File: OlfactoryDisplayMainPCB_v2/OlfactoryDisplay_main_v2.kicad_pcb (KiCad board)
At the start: 2 copper layers, 62 x 34.5 mm, 25 parts, among them J1 B2B-PH-K-S, J2 B2B-PH-K-S, J3 B2B-PH-K-S, J4 B2B-PH-K-S, J5 B2B-PH-K-S, J6 B2B-PH-K-S, J7 B2B-PH-K-S, J9 B2B-PH-K-S, U1 DMG1012UW-7, U2 DMG1012UW-7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

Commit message: rough draft of traces for V2
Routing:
- net Battery 2 In: track 0.00 -> 44.2 mm
- net Battery 1 In: track 0.00 -> 27.5 mm
- net Converter Out: track 0.00 -> 15.4 mm
- net 5V Fan Out: track 0.00 -> 7.33 mm
- net Net-(U3-G): track 0.00 -> 6.53 mm
- net Atomizer 4 Out: track 0.00 -> 6.35 mm
- net Net-(U6-G): track 0.00 -> 5.88 mm
- net Atomizer 1 Out: track 0.00 -> 5.81 mm
- net Atomizer 3 Out: track 0.00 -> 5.73 mm
- net Net-(U4-G): track 0.00 -> 5.56 mm
- net Atomizer 2 Out: track 0.00 -> 5.36 mm
- net Net-(U5-G): track 0.00 -> 4.86 mm
- net 12V Fan Out: track 0.00 -> 4.83 mm
- net Net-(U1-G): track 0.00 -> 4.44 mm
- net Net-(U2-G): track 0.00 -> 4.16 mm

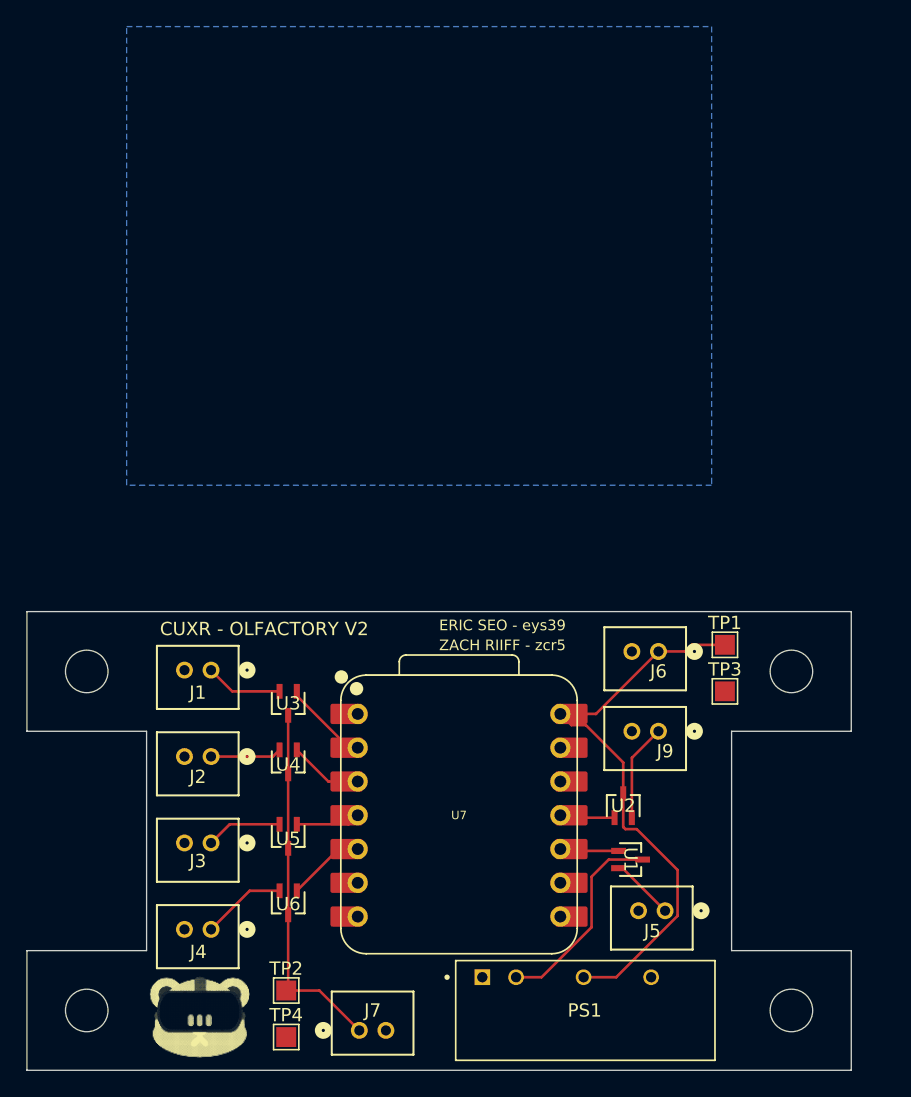
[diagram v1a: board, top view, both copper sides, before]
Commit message: Added back copper to the PCB
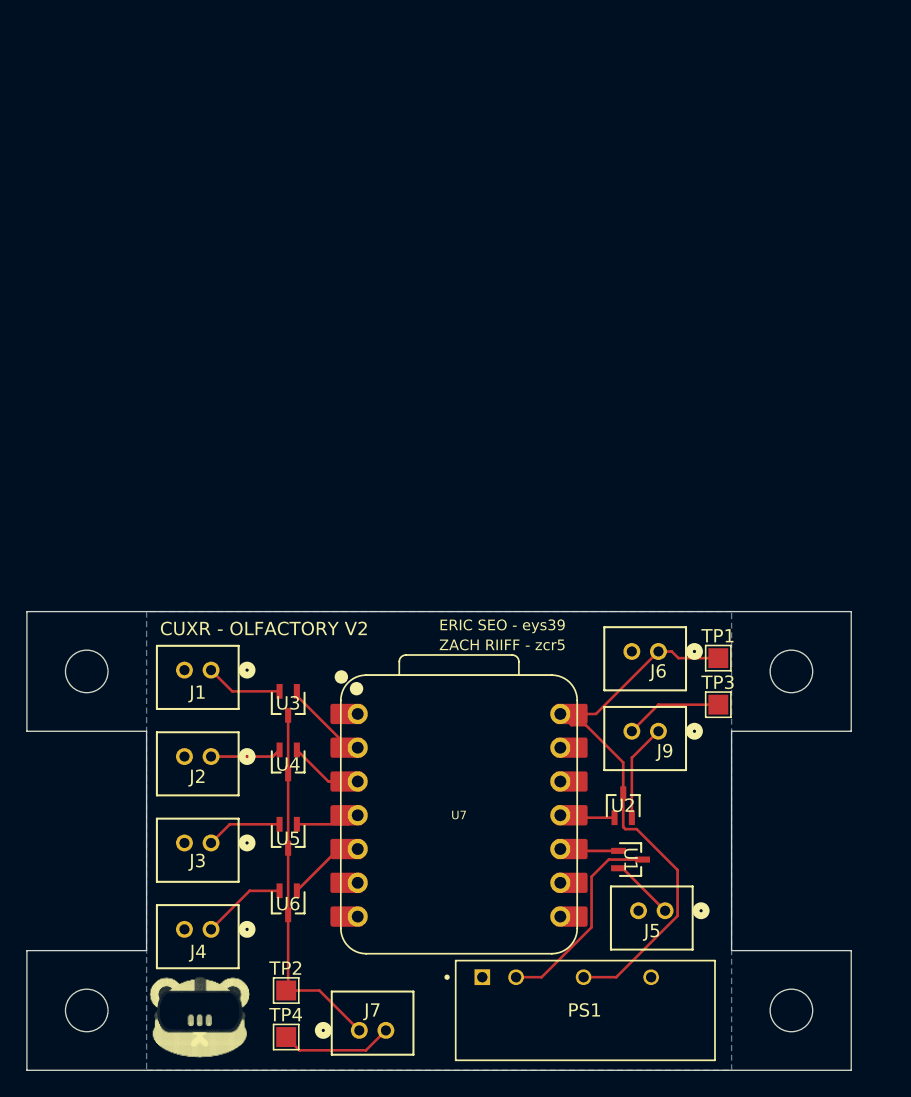
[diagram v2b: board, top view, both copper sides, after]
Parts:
- moved TP1 1.12 mm to (124.5, 99.0)
- moved TP3 1.12 mm to (124.5, 102.5)
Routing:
- net GND: track 0.45 -> 16.3 mm
- net Battery 2 In: track 44.2 -> 43.5 mm
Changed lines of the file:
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@@
 	(footprint "TestPoint:TestPoint_Pad_1.5x1.5mm"
 		(layer "F.Cu")
-		(at 125 101.5)
+		(at 124.5 102.5)
 		(descr "SMD rectangular pad as test Point, square 1.5mm side length")
 		(tags "test point SMD pad rectangle square")
@@
 	(footprint "TestPoint:TestPoint_Pad_1.5x1.5mm"
 		(layer "F.Cu")
-		(at 125 98)
+		(at 124.5 99)
 		(descr "SMD rectangular pad as test Point, square 1.5mm side length")
 		(tags "test point SMD pad rectangle square")
@@
 	)
 	(segment
-		(start 122.5 98)
-		(end 122 98.5)
+		(start 121.5 99)
+		(end 124.5 99)
 		(width 0.2)
 		(layer "F.Cu")
@@
 	)
 	(segment
-		(start 124.5 98.5)
-		(end 125 98)
+		(start 124.5 99)
+		(end 124.5 98.5)
 		(width 0.2)
 		(layer "F.Cu")
@@
 	)
 	(segment
-		(start 122 98.5)
-		(end 120.000001 98.5)
-		(width 0.2)
-		(layer "F.Cu")
-		(net 2)
-	)
-	(segment
 		(start 121.436 114.936)
 		(end 118.3598 111.8598)
@@
 	)
 	(segment
-		(start 125 98)
-		(end 122.5 98)
+		(start 113.46075 104.03925)
+		(end 112.62 103.1985)
 		(width 0.2)
 		(layer "F.Cu")
@@
 	)
 	(segment
-		(start 113.46075 104.03925)
-		(end 112.62 103.1985)
+		(start 116.823704 123)
+		(end 121.436 118.387704)
 		(width 0.2)
 		(layer "F.Cu")
@@
 	)
 	(segment
-		(start 116.823704 123)
-		(end 121.436 118.387704)
+		(start 121 98.5)
+		(end 121.5 99)
+		(width 0.2)
+		(layer "F.Cu")
+		(net 2)
+	)
+	(segment
+		(start 120.000001 98.5)
+		(end 121 98.5)
 		(width 0.2)
 		(layer "F.Cu")
@@
 	)
 	(segment
+		(start 98 128.5)
+		(end 99.5 127)
+		(width 0.2)
+		(layer "F.Cu")
+		(net 16)
+	)
+	(segment
+		(start 92 127.5)
+		(end 93 128.5)
+		(width 0.2)
+		(layer "F.Cu")
+		(net 16)
+	)
+	(segment
+		(start 120 102.5)
+		(end 124.5 102.5)
+		(width 0.2)
+		(layer "F.Cu")
+		(net 16)
+	)
+	(segment
+		(start 118 104.5)
+		(end 120 102.5)
+		(width 0.2)
+		(layer "F.Cu")
+		(net 16)
+	)
+	(segment
+		(start 93 128.5)
+		(end 98 128.5)
+		(width 0.2)
+		(layer "F.Cu")
+		(net 16)
+	)
+	(segment
 		(start 84.35 119.4017)
 		(end 84.35 119.85)
@@
 		(polygon
 			(pts
-				(xy 80 51.5) (xy 124 51.5) (xy 124 86) (xy 80 86)
+				(xy 81.5 95.5) (xy 81.5 130) (xy 125.5 130) (xy 125.5 95.5)
 			)
 		)

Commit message: Updated second version to remove 2nd battery and remove connection to 5V in seeed
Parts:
- removed J6: B2B-PH-K-S, footprints_connector:CONN2_B2B-PH-K-S_JST
- removed the REF** at (77.0, 125.5)
- removed the REF** at (130.0, 125.5)
- removed the REF** at (77.0, 100.0)
- removed the REF** at (130.0, 100.0)
- removed TP1, TP4: TestPoint, TestPoint:TestPoint_Pad_1.5x1.5mm
- added REF**: MountingHole_3.5mm, MountingHole:MountingHole_3.5mm, F.Cu at (77.0, 100.0)
- added REF**: MountingHole_3.5mm, MountingHole:MountingHole_3.5mm, F.Cu at (130.0, 100.0)
- added REF**: MountingHole_3.5mm, MountingHole:MountingHole_3.5mm, F.Cu at (77.0, 125.5)
- added REF**: MountingHole_3.5mm, MountingHole:MountingHole_3.5mm, F.Cu at (130.0, 125.5)
- moved TP3 41.0 mm to (92.0, 127.5)
- moved U4 0.70 mm to (92.1, 107.5)
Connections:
- PS1 pad 4: Battery 2 In -> Battery 1 In
- U2 pad 3: Battery 2 In -> Battery 1 In
- U7 pad 14: Battery 2 In -> unconnected-(U7-5V-Pad14)
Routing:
- net Battery 2 In: track 43.5 -> 0.00 mm
- net Battery 1 In: track 27.5 -> 67.3 mm
- net GND: track 16.3 -> 8.98 mm
- net Net-(U4-G): track 5.56 -> 2.20 mm

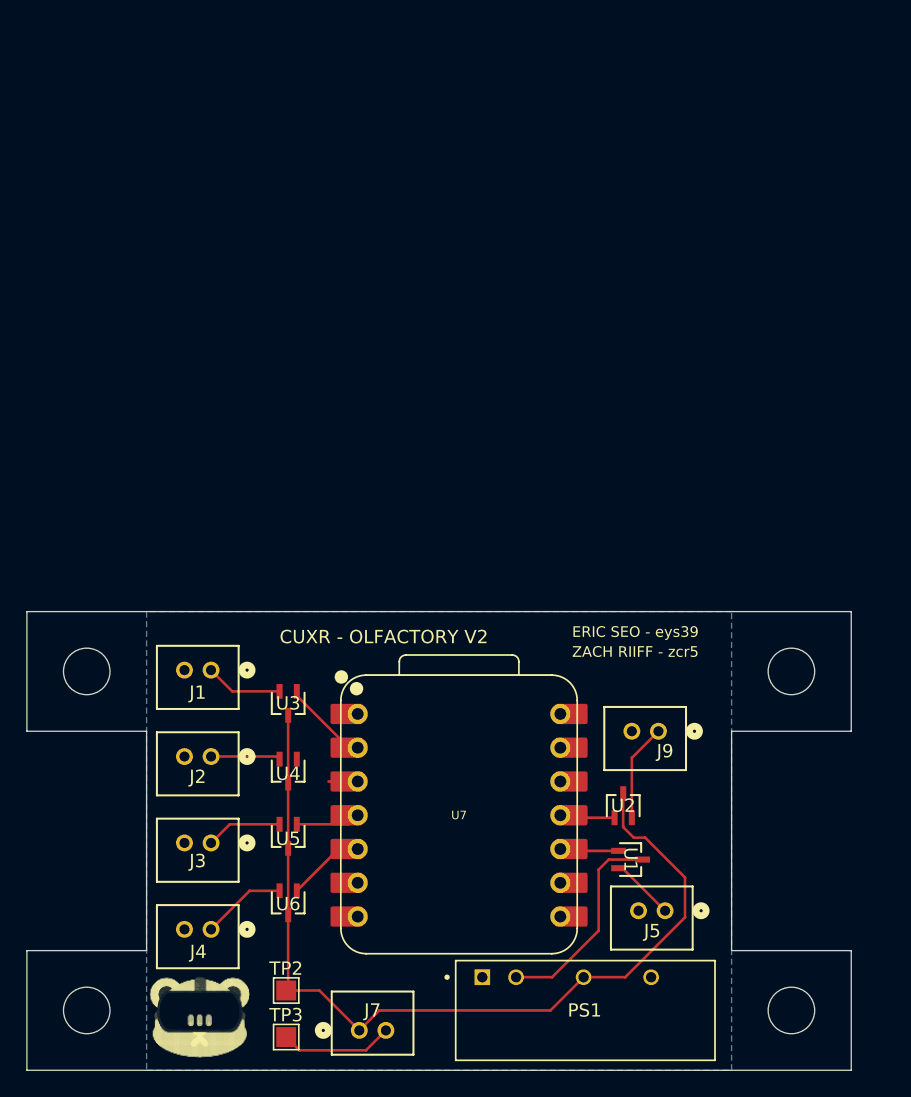
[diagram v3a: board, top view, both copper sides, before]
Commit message: Started moving fans and smellers
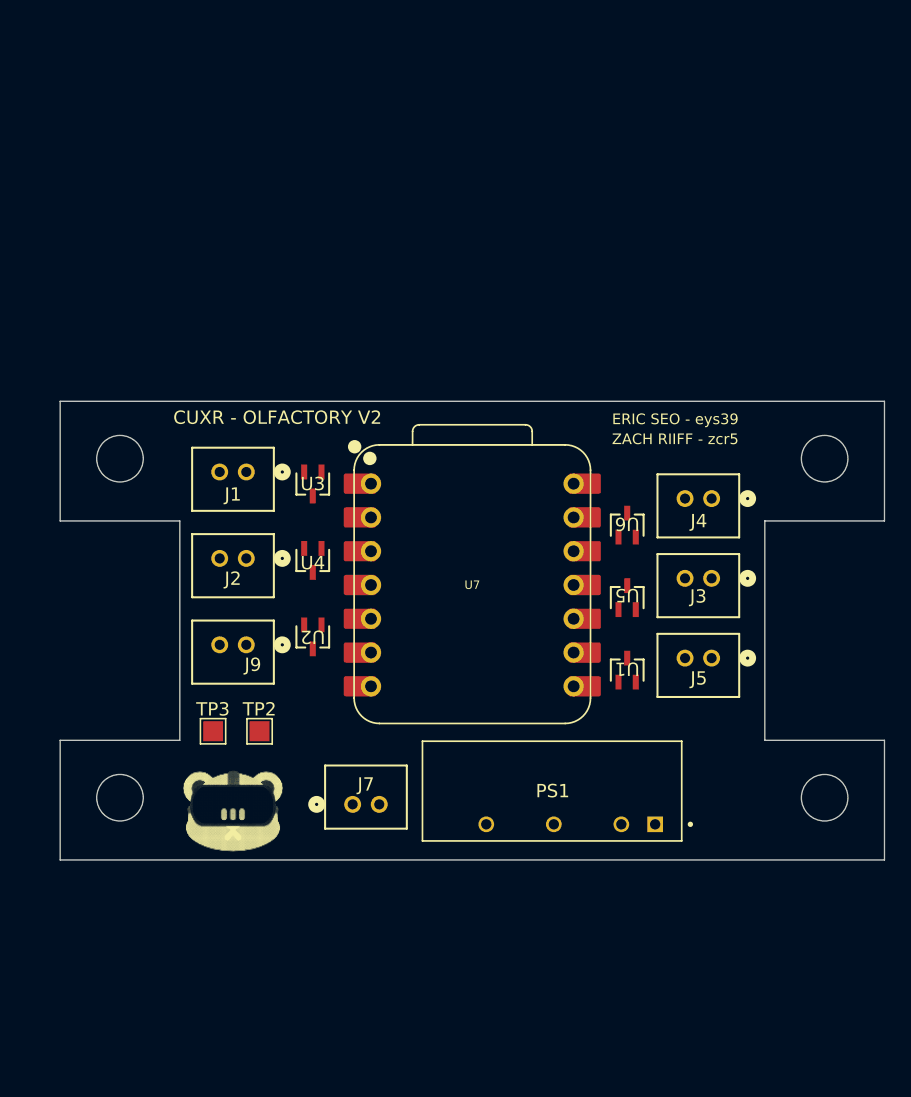
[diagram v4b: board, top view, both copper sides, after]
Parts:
- moved J4 49.7 mm to (124.0, 87.0)
- moved J3 42.6 mm to (124.0, 93.0)
- moved U6 38.2 mm to (117.7, 89.0), turned to 0 degrees
- moved J9 31.7 mm to (89.0, 98.0)
- moved U5 31.2 mm to (117.7, 94.5), turned to 0 degrees
- moved U2 26.6 mm to (94.0, 97.4), turned to 180 degrees
- moved TP3 23.6 mm to (86.5, 104.5)
- moved TP2 19.6 mm to (90.0, 104.5)
- moved J5 19.3 mm to (124.0, 99.0)
- moved U7 17.3 mm to (106.0, 93.5)
- moved J7 17.0 mm to (97.0, 110.0)
- moved PS1 16.7 mm to (112.0, 109.0), turned to 180 degrees
- moved U3 16.6 mm to (94.0, 85.9)
- moved REF** 16.2 mm to (79.5, 84.0)
- moved REF** 16.2 mm to (132.5, 84.0)
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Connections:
- U7 pad 10: Net-(U1-G) -> Net-(U5-G)
- U7 pad 11: Net-(U2-G) -> Net-(U6-G)
- U7 pad 4: Net-(U5-G) -> Net-(U2-G)
- U7 pad 5: Net-(U6-G) -> unconnected-(U7-PA8_A4_D4_SDA-Pad5)
- U7 pad 9: unconnected-(U7-PA7_A8_D8_SCK-Pad9) -> Net-(U1-G)
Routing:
- net Battery 1 In: track 67.3 -> 0.00 mm
- net Converter Out: track 15.9 -> 0.00 mm
- net GND: track 8.98 -> 0.00 mm
- net 5V Fan Out: track 7.33 -> 0.00 mm
- net Net-(U3-G): track 6.53 -> 0.00 mm
- net Atomizer 4 Out: track 6.35 -> 0.00 mm
- net Net-(U6-G): track 5.88 -> 0.00 mm
- net Atomizer 1 Out: track 5.81 -> 0.00 mm
- net Atomizer 3 Out: track 5.73 -> 0.00 mm
- net Atomizer 2 Out: track 5.23 -> 0.00 mm
- net Net-(U5-G): track 4.86 -> 0.00 mm
- net 12V Fan Out: track 4.83 -> 0.00 mm
- net Net-(U1-G): track 4.44 -> 0.00 mm
- net Net-(U2-G): track 4.16 -> 0.00 mm
- net Net-(U4-G): track 2.20 -> 0.00 mm
- removed copper zone on B.Cu, net GND

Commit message: FINISHED V2
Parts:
- moved G*** 0.18 mm to (88.0, 110.3)
- moved J1 0.18 mm to (89.0, 84.8)
- moved J2 0.18 mm to (89.0, 91.3)
- moved J3 0.18 mm to (124.0, 92.8)
- moved J4 0.18 mm to (124.0, 86.8)
- moved J5 0.18 mm to (124.0, 98.8)
- moved J7 0.18 mm to (97.0, 109.8)
- moved J9 0.18 mm to (89.0, 97.8)
- moved PS1 0.18 mm to (112.0, 108.8)
- moved REF** 0.18 mm to (79.5, 83.8)
- moved REF** 0.18 mm to (132.5, 83.8)
- moved REF** 0.18 mm to (79.5, 109.3)
- moved REF** 0.18 mm to (132.5, 109.3)
- moved TP2 0.18 mm to (90.0, 104.3)
- moved TP3 0.18 mm to (86.5, 104.3)
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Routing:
- net Battery 1 In: track 0.00 -> 71.1 mm, vias 0 -> 2
- net Converter Out: track 0.00 -> 12.7 mm
- net Atomizer 4 Out: track 0.00 -> 6.90 mm
- net GND: track 0.00 -> 6.71 mm
- net Atomizer 3 Out: track 0.00 -> 6.67 mm
- net 12V Fan Out: track 0.00 -> 6.45 mm
- net 5V Fan Out: track 0.00 -> 4.97 mm
- net Atomizer 2 Out: track 0.00 -> 4.66 mm
- net Net-(U6-G): track 0.00 -> 4.65 mm
- net Net-(U3-G): track 0.00 -> 4.62 mm
- net Atomizer 1 Out: track 0.00 -> 4.35 mm
- net Net-(U2-G): track 0.00 -> 4.20 mm
- net Net-(U1-G): track 0.00 -> 3.47 mm
- net Net-(U4-G): track 0.00 -> 2.98 mm
- net Net-(U5-G): track 0.00 -> 2.83 mm
- added copper zone on B.Cu, net GND
